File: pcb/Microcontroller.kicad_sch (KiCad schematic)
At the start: 36 parts, among them J1 PDI, SW2 START, SW3 STOP, U3 ATxmega16A4U-A, Y1 8MHz

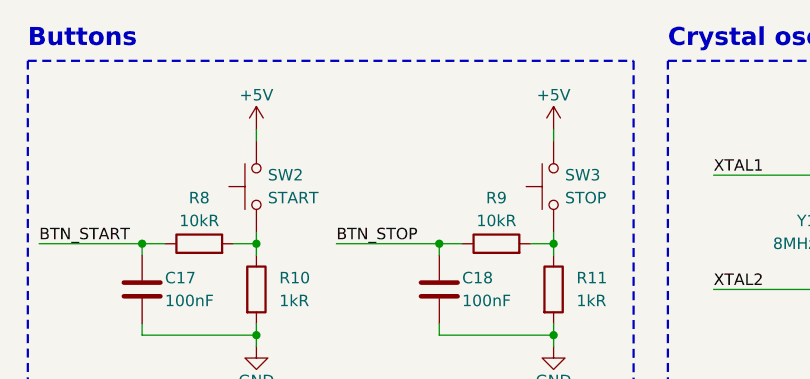
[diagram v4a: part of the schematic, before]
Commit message: [pcb] Replace 5V with 3.3V
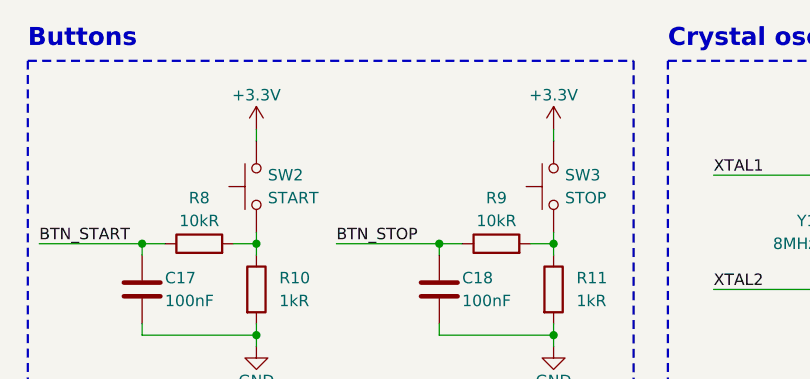
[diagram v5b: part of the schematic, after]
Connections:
- net +5V is gone; now on net +3.3V: SW2.2, SW3.2
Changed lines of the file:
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@@
+    )
+  )
+  (symbol (lib_id "power:+3.3V") (at 218.44 26.67 0) (unit 1)
+    (in_bom yes) (on_board yes) (dnp no) (fields_autoplaced)
+    (property "Reference" "#PWR016" (at 218.44 30.48 0)
+      (effects (font (size 1.27 1.27)) hide)
+    )
+    (property "Value" "+3.3V" (at 218.44 22.86 0)
+      (effects (font (size 1.27 1.27)))
+    )
+    (property "Footprint" "" (at 218.44 26.67 0)
+      (effects (font (size 1.27 1.27)) hide)
+    )
+    (property "Datasheet" "" (at 218.44 26.67 0)
+      (effects (font (size 1.27 1.27)) hide)
+    )
+    (pin "1")
+    (instances
+      (project "Autko"
+        (path "/8d5cfdec-de34-4148-9100-7125640c46f5/bbdb254f-809b-458f-9d25-868d15ad41c7"
+          (reference "#PWR016") (unit 1)
+        )
+      )
     )
   )
@@
         (path "/8d5cfdec-de34-4148-9100-7125640c46f5/bbdb254f-809b-458f-9d25-868d15ad41c7"
           (reference "R9") (unit 1)
-        )
-      )
-    )
-  )
-  (symbol (lib_id "power:+5V") (at 185.42 26.67 0) (unit 1)
-    (in_bom yes) (on_board yes) (dnp no) (fields_autoplaced)
-    (property "Reference" "#PWR015" (at 185.42 30.48 0)
-      (effects (font (size 1.27 1.27)) hide)
-    )
-    (property "Value" "+5V" (at 185.42 22.86 0)
-      (effects (font (size 1.27 1.27)))
-    )
-    (property "Footprint" "" (at 185.42 26.67 0)
-      (effects (font (size 1.27 1.27)) hide)
-    )
-    (property "Datasheet" "" (at 185.42 26.67 0)
-      (effects (font (size 1.27 1.27)) hide)
-    )
-    (pin "1")
-    (instances
-      (project "Autko"
-        (path "/8d5cfdec-de34-4148-9100-7125640c46f5/bbdb254f-809b-458f-9d25-868d15ad41c7"
-          (reference "#PWR015") (unit 1)
         )
       )
@@
     )
   )
-  (symbol (lib_id "power:+5V") (at 218.44 26.67 0) (unit 1)
-    (in_bom yes) (on_board yes) (dnp no) (fields_autoplaced)
-    (property "Reference" "#PWR016" (at 218.44 30.48 0)
-      (effects (font (size 1.27 1.27)) hide)
-    )
-    (property "Value" "+5V" (at 218.44 22.86 0)
-      (effects (font (size 1.27 1.27)))
-    )
-    (property "Footprint" "" (at 218.44 26.67 0)
-      (effects (font (size 1.27 1.27)) hide)
-    )
-    (property "Datasheet" "" (at 218.44 26.67 0)
-      (effects (font (size 1.27 1.27)) hide)
-    )
-    (pin "1")
-    (instances
-      (project "Autko"
-        (path "/8d5cfdec-de34-4148-9100-7125640c46f5/bbdb254f-809b-458f-9d25-868d15ad41c7"
-          (reference "#PWR016") (unit 1)
-        )
-      )
-    )
-  )
   (symbol (lib_id "Device:R") (at 158.75 90.17 0) (unit 1)
     (in_bom yes) (on_board yes) (dnp no)
@@
         )
       )
+    )
+  )
+  (symbol (lib_id "power:+3.3V") (at 185.42 26.67 0) (unit 1)
+    (in_bom yes) (on_board yes) (dnp no) (fields_autoplaced)
+    (property "Reference" "#PWR015" (at 185.42 30.48 0)
+      (effects (font (size 1.27 1.27)) hide)
+    )
+    (property "Value" "+3.3V" (at 185.42 22.86 0)
+      (effects (font (size 1.27 1.27)))
+    )
+    (property "Footprint" "" (at 185.42 26.67 0)
+      (effects (font (size 1.27 1.27)) hide)
+    )
+    (property "Datasheet" "" (at 185.42 26.67 0)
+      (effects (font (size 1.27 1.27)) hide)
+    )
+    (pin "1")
+    (instances
+      (project "Autko"
+        (path "/8d5cfdec-de34-4148-9100-7125640c46f5/bbdb254f-809b-458f-9d25-868d15ad41c7"
+          (reference "#PWR015") (unit 1)
+        )
+      )

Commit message: [pcb] BT routing
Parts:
- renumbered C12 to C11, C13 to C12, C14 to C13, C15 to C14, C16 to C15, C17 to C16, C18 to C17, C19 to C18
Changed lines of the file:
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@@
   (symbol (lib_id "Device:C") (at 58.42 33.02 0) (unit 1)
     (in_bom yes) (on_board yes) (dnp no)
-    (property "Reference" "C14" (at 60.96 31.75 0)
+    (property "Reference" "C13" (at 60.96 31.75 0)
       (effects (font (size 1.27 1.27)) (justify left))
     )
@@
       (project "Autko"
         (path "/8d5cfdec-de34-4148-9100-7125640c46f5/bbdb254f-809b-458f-9d25-868d15ad41c7"
+          (reference "C13") (unit 1)
+        )
+      )
+    )
+  )
+  (symbol (lib_id "power:GND") (at 35.56 39.37 0) (unit 1)
+    (in_bom yes) (on_board yes) (dnp no)
+    (property "Reference" "#PWR018" (at 35.56 45.72 0)
+      (effects (font (size 1.27 1.27)) hide)
+    )
+    (property "Value" "GND" (at 35.56 43.18 0)
+      (effects (font (size 1.27 1.27)))
+    )
+    (property "Footprint" "" (at 35.56 39.37 0)
+      (effects (font (size 1.27 1.27)) hide)
+    )
+    (property "Datasheet" "" (at 35.56 39.37 0)
+      (effects (font (size 1.27 1.27)) hide)
+    )
+    (pin "1")
+    (instances
+      (project "Autko"
+        (path "/8d5cfdec-de34-4148-9100-7125640c46f5/bbdb254f-809b-458f-9d25-868d15ad41c7"
+          (reference "#PWR018") (unit 1)
+        )
+      )
+    )
+  )
+  (symbol (lib_id "power:GND") (at 88.9 39.37 0) (unit 1)
+    (in_bom yes) (on_board yes) (dnp no)
+    (property "Reference" "#PWR019" (at 88.9 45.72 0)
+      (effects (font (size 1.27 1.27)) hide)
+    )
+    (property "Value" "GND" (at 88.9 43.18 0)
+      (effects (font (size 1.27 1.27)))
+    )
+    (property "Footprint" "" (at 88.9 39.37 0)
+      (effects (font (size 1.27 1.27)) hide)
+    )
+    (property "Datasheet" "" (at 88.9 39.37 0)
+      (effects (font (size 1.27 1.27)) hide)
+    )
+    (pin "1")
+    (instances
+      (project "Autko"
+        (path "/8d5cfdec-de34-4148-9100-7125640c46f5/bbdb254f-809b-458f-9d25-868d15ad41c7"
+          (reference "#PWR019") (unit 1)
+        )
+      )
+    )
+  )
+  (symbol (lib_id "Device:C") (at 76.2 33.02 0) (unit 1)
+    (in_bom yes) (on_board yes) (dnp no)
+    (property "Reference" "C14" (at 78.74 31.75 0)
+      (effects (font (size 1.27 1.27)) (justify left))
+    )
+    (property "Value" "100nF" (at 78.74 34.29 0)
+      (effects (font (size 1.27 1.27)) (justify left))
+    )
+    (property "Footprint" "Capacitor_SMD:C_0805_2012Metric" (at 77.1652 36.83 0)
+      (effects (font (size 1.27 1.27)) hide)
+    )
+    (property "Datasheet" "~" (at 76.2 33.02 0)
+      (effects (font (size 1.27 1.27)) hide)
+    )
+    (pin "1")
+    (pin "2")
+    (instances
+      (project "Autko"
+        (path "/8d5cfdec-de34-4148-9100-7125640c46f5/bbdb254f-809b-458f-9d25-868d15ad41c7"
           (reference "C14") (unit 1)
-        )
-      )
-    )
-  )
-  (symbol (lib_id "power:GND") (at 35.56 39.37 0) (unit 1)
-    (in_bom yes) (on_board yes) (dnp no)
-    (property "Reference" "#PWR018" (at 35.56 45.72 0)
-      (effects (font (size 1.27 1.27)) hide)
-    )
-    (property "Value" "GND" (at 35.56 43.18 0)
-      (effects (font (size 1.27 1.27)))
-    )
-    (property "Footprint" "" (at 35.56 39.37 0)
-      (effects (font (size 1.27 1.27)) hide)
-    )
-    (property "Datasheet" "" (at 35.56 39.37 0)
-      (effects (font (size 1.27 1.27)) hide)
-    )
-    (pin "1")
-    (instances
-      (project "Autko"
-        (path "/8d5cfdec-de34-4148-9100-7125640c46f5/bbdb254f-809b-458f-9d25-868d15ad41c7"
-          (reference "#PWR018") (unit 1)
-        )
-      )
-    )
-  )
-  (symbol (lib_id "power:GND") (at 88.9 39.37 0) (unit 1)
-    (in_bom yes) (on_board yes) (dnp no)
-    (property "Reference" "#PWR019" (at 88.9 45.72 0)
-      (effects (font (size 1.27 1.27)) hide)
-    )
-    (property "Value" "GND" (at 88.9 43.18 0)
-      (effects (font (size 1.27 1.27)))
-    )
-    (property "Footprint" "" (at 88.9 39.37 0)
-      (effects (font (size 1.27 1.27)) hide)
-    )
-    (property "Datasheet" "" (at 88.9 39.37 0)
-      (effects (font (size 1.27 1.27)) hide)
-    )
-    (pin "1")
-    (instances
-      (project "Autko"
-        (path "/8d5cfdec-de34-4148-9100-7125640c46f5/bbdb254f-809b-458f-9d25-868d15ad41c7"
-          (reference "#PWR019") (unit 1)
-        )
-      )
-    )
-  )
-  (symbol (lib_id "Device:C") (at 76.2 33.02 0) (unit 1)
-    (in_bom yes) (on_board yes) (dnp no)
-    (property "Reference" "C15" (at 78.74 31.75 0)
-      (effects (font (size 1.27 1.27)) (justify left))
-    )
-    (property "Value" "100nF" (at 78.74 34.29 0)
-      (effects (font (size 1.27 1.27)) (justify left))
-    )
-    (property "Footprint" "Capacitor_SMD:C_0805_2012Metric" (at 77.1652 36.83 0)
-      (effects (font (size 1.27 1.27)) hide)
-    )
-    (property "Datasheet" "~" (at 76.2 33.02 0)
-      (effects (font (size 1.27 1.27)) hide)
-    )
-    (pin "1")
-    (pin "2")
-    (instances
-      (project "Autko"
-        (path "/8d5cfdec-de34-4148-9100-7125640c46f5/bbdb254f-809b-458f-9d25-868d15ad41c7"
-          (reference "C15") (unit 1)
         )
       )
@@
   (symbol (lib_id "Device:C") (at 205.74 44.45 0) (unit 1)
     (in_bom yes) (on_board yes) (dnp no)
-    (property "Reference" "C18" (at 208.28 43.18 0)
+    (property "Reference" "C17" (at 208.28 43.18 0)
       (effects (font (size 1.27 1.27)) (justify left))
     )
@@
       (project "Autko"
         (path "/8d5cfdec-de34-4148-9100-7125640c46f5/bbdb254f-809b-458f-9d25-868d15ad41c7"
-          (reference "C18") (unit 1)
+          (reference "C17") (unit 1)
         )
       )
@@
   (symbol (lib_id "Device:C") (at 46.99 33.02 0) (unit 1)
     (in_bom yes) (on_board yes) (dnp no)
-    (property "Reference" "C13" (at 49.53 31.75 0)
+    (property "Reference" "C12" (at 49.53 31.75 0)
       (effects (font (size 1.27 1.27)) (justify left))
     )
@@
       (project "Autko"
         (path "/8d5cfdec-de34-4148-9100-7125640c46f5/bbdb254f-809b-458f-9d25-868d15ad41c7"
-          (reference "C13") (unit 1)
+          (reference "C12") (unit 1)
         )
       )
@@
   (symbol (lib_id "Device:C") (at 172.72 44.45 0) (unit 1)
     (in_bom yes) (on_board yes) (dnp no)
-    (property "Reference" "C17" (at 175.26 43.18 0)
+    (property "Reference" "C16" (at 175.26 43.18 0)
       (effects (font (size 1.27 1.27)) (justify left))
     )
@@
       (project "Autko"
         (path "/8d5cfdec-de34-4148-9100-7125640c46f5/bbdb254f-809b-458f-9d25-868d15ad41c7"
-          (reference "C17") (unit 1)
+          (reference "C16") (unit 1)
         )
       )
@@
   (symbol (lib_id "Device:C_Polarized") (at 88.9 33.02 0) (unit 1)
     (in_bom yes) (on_board yes) (dnp no)
-    (property "Reference" "C16" (at 91.44 31.75 0)
+    (property "Reference" "C15" (at 91.44 31.75 0)
       (effects (font (size 1.27 1.27)) (justify left))
     )
@@
       (project "Autko"
         (path "/8d5cfdec-de34-4148-9100-7125640c46f5/bbdb254f-809b-458f-9d25-868d15ad41c7"
-          (reference "C16") (unit 1)
+          (reference "C15") (unit 1)
         )
       )
@@
   (symbol (lib_id "Device:C") (at 257.81 44.45 90) (unit 1)
     (in_bom yes) (on_board yes) (dnp no)
-    (property "Reference" "C19" (at 257.81 38.1 90)
+    (property "Reference" "C18" (at 257.81 38.1 90)
       (effects (font (size 1.27 1.27)))
     )
@@
       (project "Autko"
         (path "/8d5cfdec-de34-4148-9100-7125640c46f5/bbdb254f-809b-458f-9d25-868d15ad41c7"
-          (reference "C19") (unit 1)
+          (reference "C18") (unit 1)
         )
       )
@@
   (symbol (lib_id "Device:C") (at 35.56 33.02 0) (unit 1)
     (in_bom yes) (on_board yes) (dnp no)
-    (property "Reference" "C12" (at 38.1 31.75 0)
+    (property "Reference" "C11" (at 38.1 31.75 0)
       (effects (font (size 1.27 1.27)) (justify left))
     )
@@
       (project "Autko"
         (path "/8d5cfdec-de34-4148-9100-7125640c46f5/bbdb254f-809b-458f-9d25-868d15ad41c7"
-          (reference "C12") (unit 1)
-        )
-      )
+          (reference "C11") (unit 1)
+        )
+      )

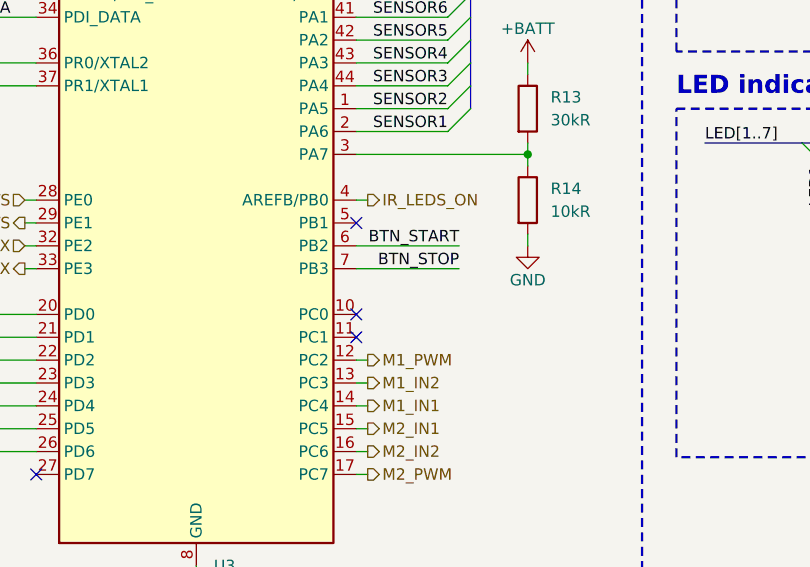
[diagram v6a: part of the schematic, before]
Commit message: [pcb] Buttons routed
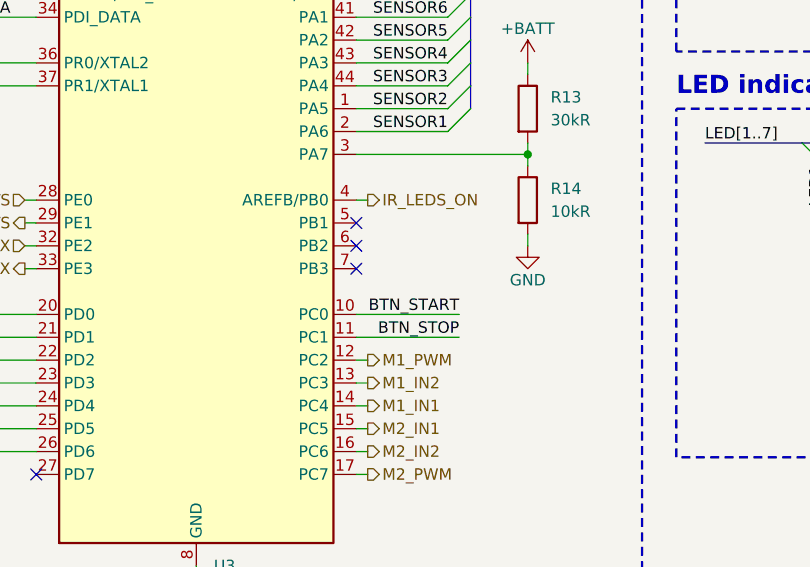
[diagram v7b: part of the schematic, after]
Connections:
- net BTN_START: now also U3.10 (PC0); no longer U3.6 (PB2)
- net BTN_STOP: now also U3.11 (PC1); no longer U3.7 (PB3)
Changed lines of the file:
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@@
   (junction (at 148.59 95.25) (diameter 0) (color 0 0 0 0)
   )
-  (no_connect (at 86.36 87.63))
+  (no_connect (at 86.36 80.01))
   (no_connect (at 50.8 105.41))
   (no_connect (at 86.36 77.47))
-  (no_connect (at 86.36 90.17))
+  (no_connect (at 86.36 82.55))
   (no_connect (at 135.89 39.37))
   (no_connect (at 148.59 39.37))
@@
     (stroke (width 0) (type default))
   )
-  (wire (pts (xy 86.36 82.55) (xy 97.79 82.55))
+  (wire (pts (xy 86.36 90.17) (xy 97.79 90.17))
     (stroke (width 0) (type default))
   )
@@
     (stroke (width 0) (type default))
   )
-  (wire (pts (xy 86.36 80.01) (xy 97.79 80.01))
+  (wire (pts (xy 86.36 87.63) (xy 97.79 87.63))
     (stroke (width 0) (type default))
   )
@@
     (effects (font (size 1.27 1.27)) (justify left bottom))
   )
-  (label "BTN_STOP" (at 97.79 82.55 180) (fields_autoplaced)
-    (effects (font (size 1.27 1.27)) (justify right bottom))
-  )
-  (label "BTN_START" (at 97.79 80.01 180) (fields_autoplaced)
-    (effects (font (size 1.27 1.27)) (justify right bottom))
-  )
+  (label "BTN_STOP" (at 97.79 90.17 180) (fields_autoplaced)
+    (effects (font (size 1.27 1.27)) (justify right bottom))
+  )
+  (label "BTN_START" (at 97.79 87.63 180) (fields_autoplaced)
+    (effects (font (size 1.27 1.27)) (justify right bottom))
+  )

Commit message: [pcb] Boost converter routing
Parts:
- SW2, SW3: footprint Button_Switch_THT:SW_PUSH_6mm_H5mm -> Autko:12mm_tact_switch
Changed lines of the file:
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@@
       (effects (font (size 1.27 1.27)) (justify right))
     )
-    (property "Footprint" "Button_Switch_THT:SW_PUSH_6mm_H5mm" (at 180.34 33.02 0)
+    (property "Footprint" "Autko:12mm_tact_switch" (at 180.34 33.02 0)
       (effects (font (size 1.27 1.27)) hide)
     )
@@
       (effects (font (size 1.27 1.27)) (justify right))
     )
-    (property "Footprint" "Button_Switch_THT:SW_PUSH_6mm_H5mm" (at 213.36 33.02 0)
-      (effects (font (size 1.27 1.27)) hide)
-    )
+    (property "Footprint" "Autko:12mm_tact_switch" (at 213.36 33.02 0)
+      (effects (font (size 1.27 1.27)) hide)
+    )
